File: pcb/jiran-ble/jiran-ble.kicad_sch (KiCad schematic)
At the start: 167 parts, among them J1 BATT, J2 USB-C Connector, J3 SWD, J4 BATT, J5 USB-C Connector, J6 SWD, Q1 SI2301CDS-T1-GE3, Q2 SI2301CDS-T1-GE3, SW1 SW_PUSH, SW10 SW_Push, SW11 SW_Push, SW12 SW_Push, SW13 SW_Push, SW14 SW_Push, SW15 SW_Push, SW16 SW_Push, SW17 SW_Push, SW18 SW_Push, SW19 SW_Push, SW2 SW_DPDT_x2, SW20 SW_Push, SW21 SW_Push, SW22 SW_Push, SW23 SW_Push, SW24 SW_Push, SW25 SW_Push, SW26 SW_Push, SW27 SW_Push, SW28 SW_Push, SW29 SW_Push, SW3 SW_Push, SW30 SW_Push, SW31 SW_PUSH, SW32 SW_Push, SW33 SW_Push, SW34 SW_Push, SW35 SW_Push, SW36 SW_Push, SW37 SW_Push, SW38 SW_Push, SW39 SW_Push, SW4 SW_Push, SW40 SW_Push, SW41 SW_Push, SW42 SW_Push, SW43 SW_Push, SW44 SW_Push, SW45 SW_Push, SW46 SW_Push, SW47 SW_Push, SW48 SW_Push, SW49 SW_Push, SW5 SW_Push, SW50 SW_Push, SW51 SW_Push, SW52 SW_Push, SW53 SW_Push, SW54 SW_Push, SW55 SW_Push, SW56 SW_Push, SW57 SW_Push, SW58 SW_Push, SW59 SW_Push, SW6 SW_Push, SW7 SW_Push, SW8 SW_Push, SW9 SW_Push, U1 HOLYIOT-18010-NRF52840_simple, U2 XC6220B331MR-G, U3 TP4054, U4 HOLYIOT-18010-NRF52840_simple, U5 XC6220B331MR-G, U6 TP4054

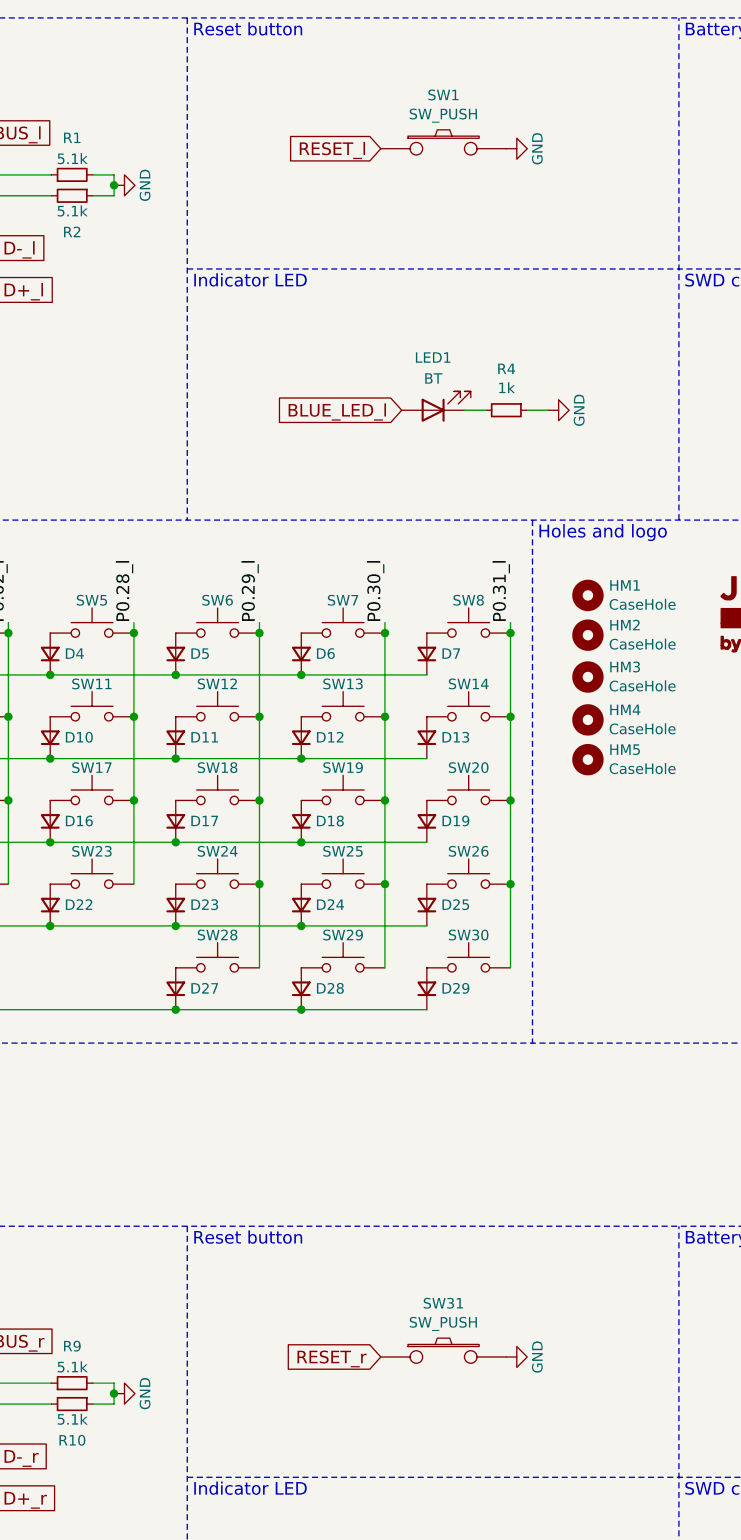
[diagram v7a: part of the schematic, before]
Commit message: Replace tact button with pins
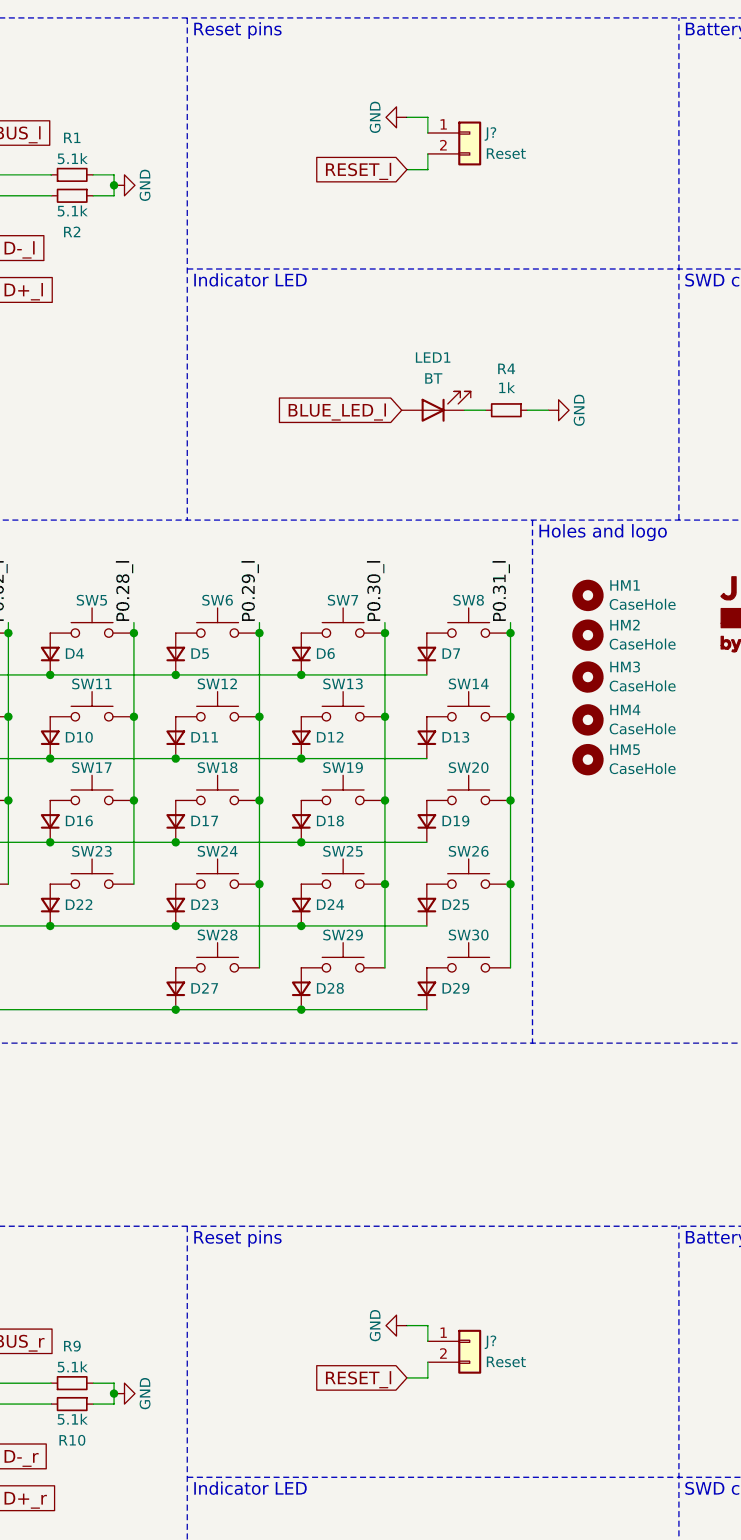
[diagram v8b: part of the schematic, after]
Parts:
- removed SW1, SW31: SW_PUSH, jiran-ble:Switch_SMD_Tact_K2-118, symbol jiran-ble-rescue:SW_PUSH-keyboard_parts-candy-rescue
- added J? (x2): Reset, symbol Connector_Generic:Conn_01x02
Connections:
- net GND: now also J?.1 (Pin_1), J?.1 (Pin_1)
- net RESET_l: now also J?.2 (Pin_2), J?.2 (Pin_2)
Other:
- note added: "Reset pins"
- note removed: "Reset button"
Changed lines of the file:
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@@
     (stroke (width 0) (type solid) (color 0 0 0 0))
   )
+  (wire (pts (xy 189.23 24.765) (xy 191.77 24.765))
+    (stroke (width 0) (type solid) (color 0 0 0 0))
+  )
+  (wire (pts (xy 189.23 31.115) (xy 191.77 31.115))
+    (stroke (width 0) (type solid) (color 0 0 0 0))
+  )
+  (wire (pts (xy 189.23 171.45) (xy 191.77 171.45))
+    (stroke (width 0) (type solid) (color 0 0 0 0))
+  )
+  (wire (pts (xy 189.23 177.8) (xy 191.77 177.8))
+    (stroke (width 0) (type solid) (color 0 0 0 0))
+  )
+  (wire (pts (xy 191.77 24.765) (xy 191.77 26.67))
+    (stroke (width 0) (type solid) (color 0 0 0 0))
+  )
+  (wire (pts (xy 191.77 29.21) (xy 191.77 31.115))
+    (stroke (width 0) (type solid) (color 0 0 0 0))
+  )
+  (wire (pts (xy 191.77 171.45) (xy 191.77 173.355))
+    (stroke (width 0) (type solid) (color 0 0 0 0))
+  )
+  (wire (pts (xy 191.77 175.895) (xy 191.77 177.8))
+    (stroke (width 0) (type solid) (color 0 0 0 0))
+  )
   (wire (pts (xy 198.755 60.325) (xy 196.215 60.325))
     (stroke (width 0) (type solid) (color 0 0 0 0))
@@
     (effects (font (size 1.5494 1.5494)) (justify left bottom))
   )
-  (text "Reset button" (at 163.195 15.24 0)
+  (text "Reset pins" (at 163.195 15.24 0)
     (effects (font (size 1.524 1.524)) (justify left bottom))
   )
@@
     (effects (font (size 1.524 1.524)) (justify left bottom))
   )
-  (text "Reset button" (at 163.195 161.925 0)
+  (text "Reset pins" (at 163.195 161.925 0)
     (effects (font (size 1.524 1.524)) (justify left bottom))
   )
@@
     )
   )
-  (global_label "RESET_l" (shape input) (at 186.055 28.575 180)
+  (global_label "BLUE_LED_l" (shape input) (at 188.595 60.325 180)
     (effects (font (size 1.524 1.524)) (justify right))
     (property "Intersheet References" "${INTERSHEET_REFS}" (id 0) (at 0 0 0)
@@
     )
   )
-  (global_label "RESET_r" (shape input) (at 186.055 175.26 180)
+  (global_label "BLUE_LED_r" (shape input) (at 188.595 207.01 180)
     (effects (font (size 1.524 1.524)) (justify right))
     (property "Intersheet References" "${INTERSHEET_REFS}" (id 0) (at 0 0 0)
@@
     )
   )
-  (global_label "BLUE_LED_l" (shape input) (at 188.595 60.325 180)
+  (global_label "RESET_l" (shape input) (at 189.23 31.115 180)
     (effects (font (size 1.524 1.524)) (justify right))
-    (property "Intersheet References" "${INTERSHEET_REFS}" (id 0) (at 0 0 0)
+    (property "Intersheet References" "${INTERSHEET_REFS}" (id 0) (at 3.175 2.54 0)
       (effects (font (size 1.27 1.27)) hide)
     )
   )
-  (global_label "BLUE_LED_r" (shape input) (at 188.595 207.01 180)
+  (global_label "RESET_l" (shape input) (at 189.23 177.8 180)
     (effects (font (size 1.524 1.524)) (justify right))
-    (property "Intersheet References" "${INTERSHEET_REFS}" (id 0) (at 0 0 0)
+    (property "Intersheet References" "${INTERSHEET_REFS}" (id 0) (at 3.175 149.225 0)
       (effects (font (size 1.27 1.27)) hide)
     )
@@
     (pin "1")
   )
-  (symbol (lib_id "power:GND") (at 201.295 28.575 90) (unit 1)
+  (symbol (lib_id "power:GND") (at 189.23 24.765 270) (unit 1)
     (in_bom yes) (on_board yes)
-    (property "Reference" "#PWR03" (id 0) (at 207.645 28.575 0)
+    (property "Reference" "#PWR03" (id 0) (at 182.88 24.765 0)
       (effects (font (size 1.27 1.27)) hide)
     )
-    (property "Value" "GND" (id 1) (at 205.105 28.575 0))
-    (property "Footprint" "" (id 2) (at 201.295 28.575 0)
+    (property "Value" "GND" (id 1) (at 185.42 24.765 0))
+    (property "Footprint" "" (id 2) (at 189.23 24.765 0)
       (effects (font (size 1.27 1.27)) hide)
     )
-    (property "Datasheet" "" (id 3) (at 201.295 28.575 0)
+    (property "Datasheet" "" (id 3) (at 189.23 24.765 0)
       (effects (font (size 1.27 1.27)) hide)
     )
     (pin "1")
   )
-  (symbol (lib_id "power:GND") (at 201.295 175.26 90) (unit 1)
+  (symbol (lib_id "power:GND") (at 189.23 171.45 270) (unit 1)
     (in_bom yes) (on_board yes)
-    (property "Reference" "#PWR019" (id 0) (at 207.645 175.26 0)
+    (property "Reference" "#PWR?" (id 0) (at 182.88 171.45 0)
       (effects (font (size 1.27 1.27)) hide)
     )
-    (property "Value" "GND" (id 1) (at 205.105 175.26 0))
-    (property "Footprint" "" (id 2) (at 201.295 175.26 0)
+    (property "Value" "GND" (id 1) (at 185.42 171.45 0))
+    (property "Footprint" "" (id 2) (at 189.23 171.45 0)
       (effects (font (size 1.27 1.27)) hide)
     )
-    (property "Datasheet" "" (id 3) (at 201.295 175.26 0)
+    (property "Datasheet" "" (id 3) (at 189.23 171.45 0)
       (effects (font (size 1.27 1.27)) hide)
     )
@@
     (pin "2")
   )
+  (symbol (lib_id "Connector_Generic:Conn_01x02") (at 196.85 26.67 0) (unit 1)
+    (in_bom yes) (on_board yes)
+    (property "Reference" "J?" (id 0) (at 198.755 26.6699 0)
+      (effects (font (size 1.27 1.27)) (justify left))
+    )
+    (property "Value" "Reset" (id 1) (at 198.755 29.2099 0)
+      (effects (font (size 1.27 1.27)) (justify left))
+    )
+    (property "Footprint" "" (id 2) (at 196.85 26.67 0)
+      (effects (font (size 1.27 1.27)) hide)
+    )
+    (property "Datasheet" "~" (id 3) (at 196.85 26.67 0)
+      (effects (font (size 1.27 1.27)) hide)
+    )
+    (pin "1")
+    (pin "2")
+  )
+  (symbol (lib_id "Connector_Generic:Conn_01x02") (at 196.85 173.355 0) (unit 1)
+    (in_bom yes) (on_board yes)
+    (property "Reference" "J?" (id 0) (at 198.755 173.3549 0)
+      (effects (font (size 1.27 1.27)) (justify left))
+    )
+    (property "Value" "Reset" (id 1) (at 198.755 175.8949 0)
+      (effects (font (size 1.27 1.27)) (justify left))
+    )
+    (property "Footprint" "" (id 2) (at 196.85 173.355 0)
+      (effects (font (size 1.27 1.27)) hide)
+    )
+    (property "Datasheet" "~" (id 3) (at 196.85 173.355 0)
+      (effects (font (size 1.27 1.27)) hide)
+    )
+    (pin "1")
+    (pin "2")
+  )
   (symbol (lib_id "Connector_Generic:Conn_01x02") (at 258.445 26.035 0) (unit 1)
     (in_bom yes) (on_board yes)
@@
     (pin "2")
   )
-  (symbol (lib_id "jiran-ble-rescue:SW_PUSH-keyboard_parts-candy-rescue") (at 193.675 28.575 0) (unit 1)
-    (in_bom yes) (on_board yes)
-    (property "Reference" "SW1" (id 0) (at 193.675 22.098 0))
-    (property "Value" "SW_PUSH" (id 1) (at 193.675 24.4094 0))
-    (property "Footprint" "jiran-ble:Switch_SMD_Tact_K2-118" (id 2) (at 193.675 28.575 0)
-      (effects (font (size 1.524 1.524)) hide)
-    )
-    (property "Datasheet" "" (id 3) (at 193.675 28.575 0)
-      (effects (font (size 1.524 1.524)))
-    )
-    (pin "1")
-    (pin "2")
-  )
-  (symbol (lib_id "jiran-ble-rescue:SW_PUSH-keyboard_parts-candy-rescue") (at 193.675 175.26 0) (unit 1)
-    (in_bom yes) (on_board yes)
-    (property "Reference" "SW31" (id 0) (at 193.675 168.783 0))
-    (property "Value" "SW_PUSH" (id 1) (at 193.675 171.0944 0))
-    (property "Footprint" "jiran-ble:Switch_SMD_Tact_K2-118" (id 2) (at 193.675 175.26 0)
-      (effects (font (size 1.524 1.524)) hide)
-    )
-    (property "Datasheet" "" (id 3) (at 193.675 175.26 0)
-      (effects (font (size 1.524 1.524)))
-    )
-    (pin "1")
-    (pin "2")
-  )
   (symbol (lib_id "Switch:SW_DPDT_x2") (at 325.755 47.625 0) (unit 1)
     (in_bom yes) (on_board yes)
@@
       (reference "#PWR018") (unit 1) (value "GND") (footprint "")
     )
-    (path "/00000000-0000-0000-0000-00006130bc6c"
-      (reference "#PWR019") (unit 1) (value "GND") (footprint "")
-    )
     (path "/00000000-0000-0000-0000-00006130bf2d"
       (reference "#PWR020") (unit 1) (value "GND") (footprint "")
@@
       (reference "#PWR033") (unit 1) (value "GND") (footprint "")
     )
+    (path "/b1196850-b82d-4a3b-a8cf-13081f85b0df"
+      (reference "#PWR?") (unit 1) (value "GND") (footprint "")
+    )
     (path "/00000000-0000-0000-0000-00006052c804"
       (reference "C1") (unit 1) (value "10uF") (footprint "jiran-ble:Capacitor_SMD_0402")
@@
       (reference "J6") (unit 1) (value "SWD") (footprint "jiran-ble:Connector_THT_1x4_2.54")
     )
+    (path "/59532b12-9d49-47a2-8f01-db8fb5f32980"
+      (reference "J?") (unit 1) (value "Reset") (footprint "")
+    )
+    (path "/b536eaa2-0231-4afd-ae0a-aa29a8e8048c"
+      (reference "J?") (unit 1) (value "Reset") (footprint "")
+    )
     (path "/00000000-0000-0000-0000-00005e81e127"
       (reference "LED1") (unit 1) (value "BT") (footprint "jiran-ble:LED_SMD_0402")
@@
       (reference "R16") (unit 1) (value "10k") (footprint "jiran-ble:Resistor_SMD_0402")
     )
-    (path "/00000000-0000-0000-0000-00005e9908fe"
-      (reference "SW1") (unit 1) (value "SW_PUSH") (footprint "jiran-ble:Switch_SMD_Tact_K2-118")
-    )
     (path "/b96e24a5-8cbd-40bf-b134-58cd8137e945"
       (reference "SW2") (unit 1) (value "SW_DPDT_x2") (footprint "")
@@
       (reference "SW30") (unit 1) (value "SW_Push") (footprint "jiran-ble:Switch_Mx_Hotswap_1u")
     )
-    (path "/00000000-0000-0000-0000-00006130bc65"
-      (reference "SW31") (unit 1) (value "SW_PUSH") (footprint "jiran-ble:Switch_SMD_Tact_K2-118")
-    )
     (path "/00000000-0000-0000-0000-00006130bef7"
